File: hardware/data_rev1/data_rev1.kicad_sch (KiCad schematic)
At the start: 24 parts, among them J1 AudioJack3, J2 AudioJack3, J3 BOARD, SW1 PTS636, SW2 PTS636, SW3 PTS636, U1 CAP1206-x-AIA, U2 Pico

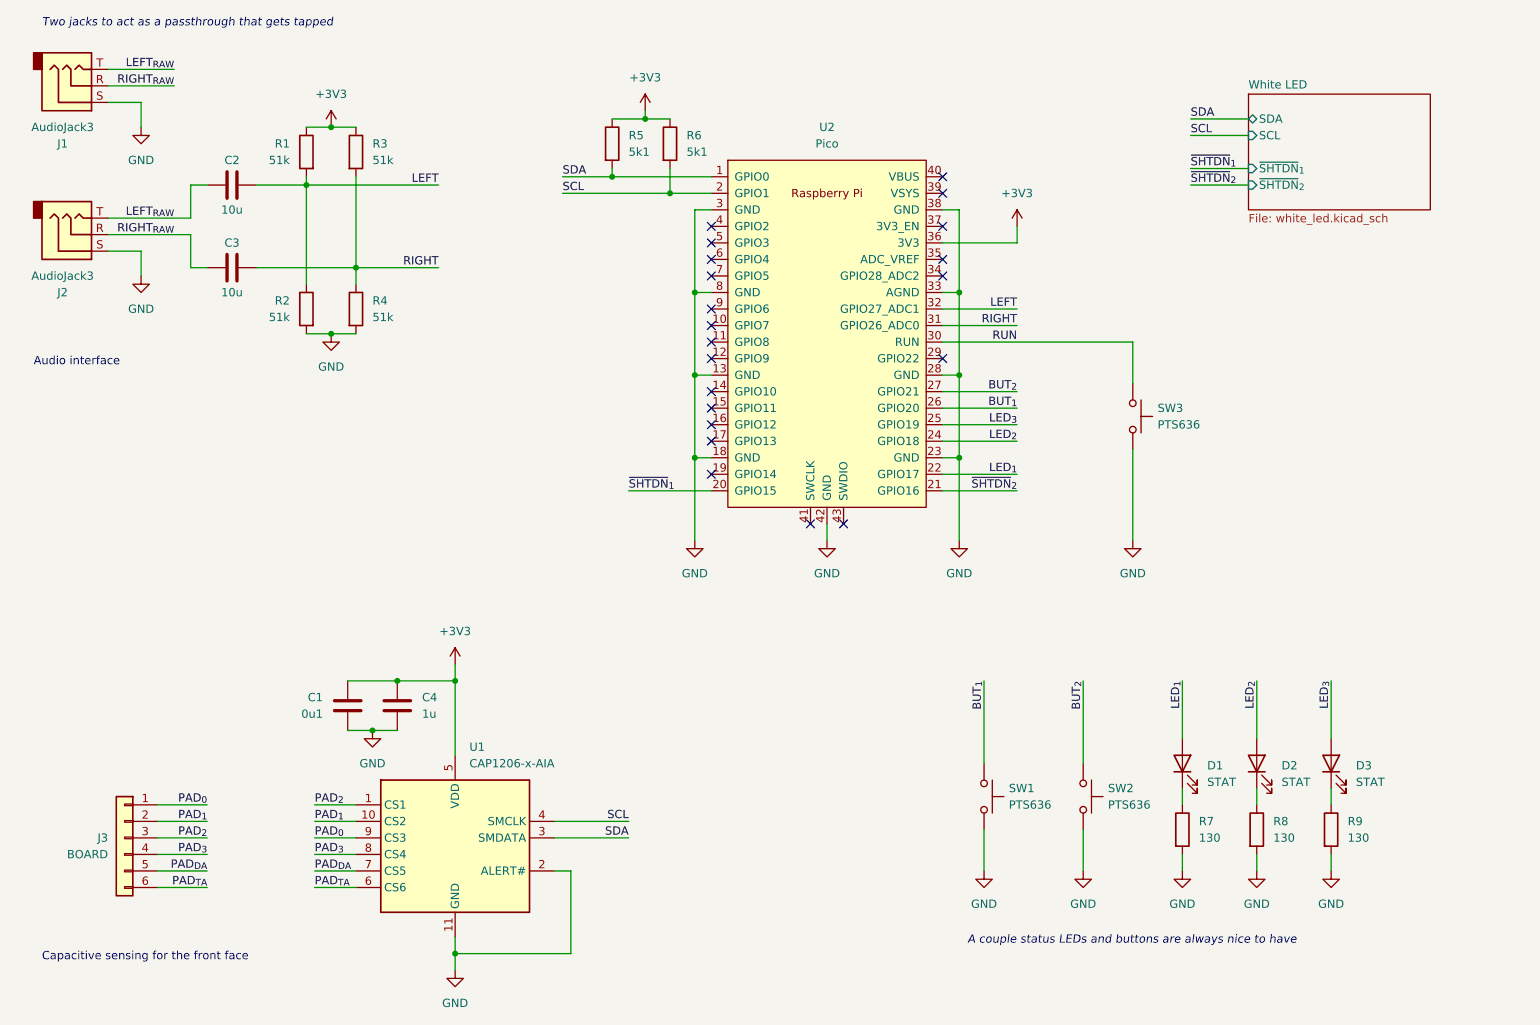
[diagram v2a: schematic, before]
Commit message: Moved audio jacks to the side. Ordered.
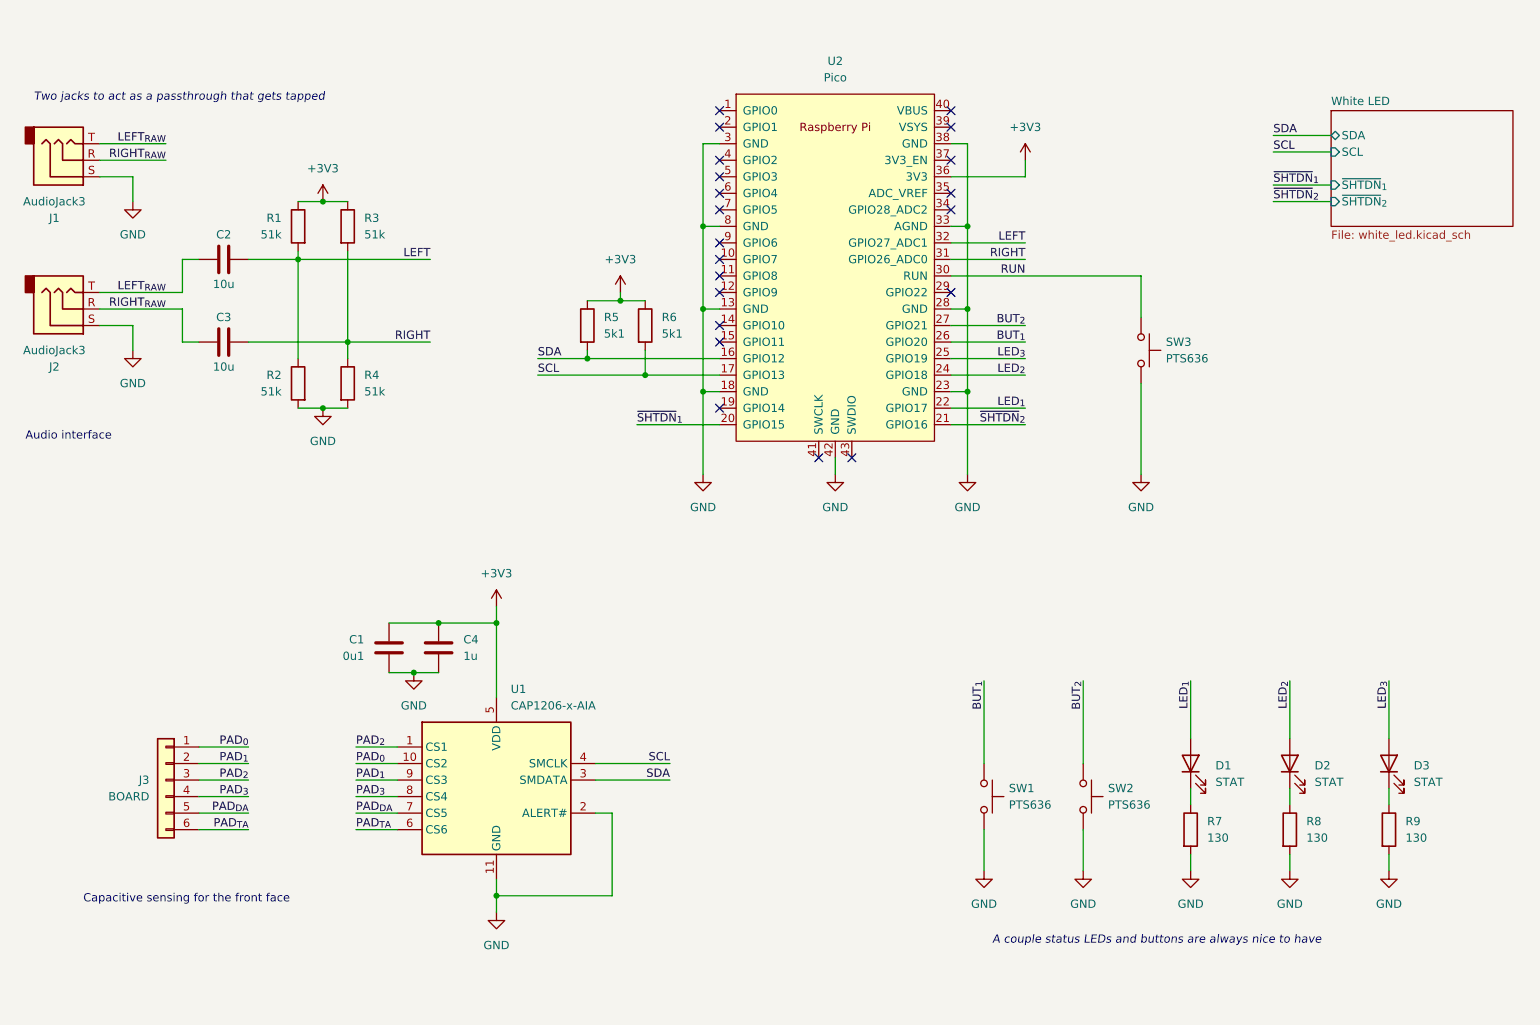
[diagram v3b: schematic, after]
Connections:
- net PAD_{0}: now also U1.10 (CS2); no longer U1.9 (CS3)
- net PAD_{1}: now also U1.9 (CS3); no longer U1.10 (CS2)
- net SCL: now also U2.17 (GPIO13); no longer U2.2 (GPIO1)
- net SDA: now also U2.16 (GPIO12); no longer U2.1 (GPIO0)
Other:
- moved on the sheet: C1, C2, C3, C4, D1, D2, D3, J1, J2, J3, R1, R2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

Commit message: Finalized BOM
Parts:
- R5, R6: value 5k1 -> 5k9
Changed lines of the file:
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@@
   (title_block
     (title "DATA Loading")
-    (date "2024-02-17")
-    (rev "0.2")
+    (date "2024-02-19")
+    (rev "0.3")
     (company "Savo Bajic")
   )
@@
       (effects (font (size 1.27 1.27)) (justify left))
     )
-    (property "Value" "5k1" (at 121.92 72.39 0)
+    (property "Value" "5k9" (at 121.92 72.39 0)
       (effects (font (size 1.27 1.27)) (justify left))
     )
@@
       (effects (font (size 1.27 1.27)) (justify left))
     )
-    (property "Value" "5k1" (at 113.03 72.39 0)
-      (effects (font (size 1.27 1.27)) (justify left))
-    )
+    (property "Value" "5k9" (at 113.03 72.39 0)
+      (effects (font (size 1.27 1.27)) (justify left))
+    )

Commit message: Moved to KiCad 8.0.0
Also added value for right angle LEDs toi be seperate of the head on ones
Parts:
- C2, C3: footprint Resistor_SMD:R_0805_2012Metric -> Capacitor_SMD:C_0805_2012Metric
